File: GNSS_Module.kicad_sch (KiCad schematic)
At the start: 23 parts, among them J2 FTDI_Conn, J4 GPS_Conn, J5 GPS_Conn, U11 ublox_SAM-M8Q

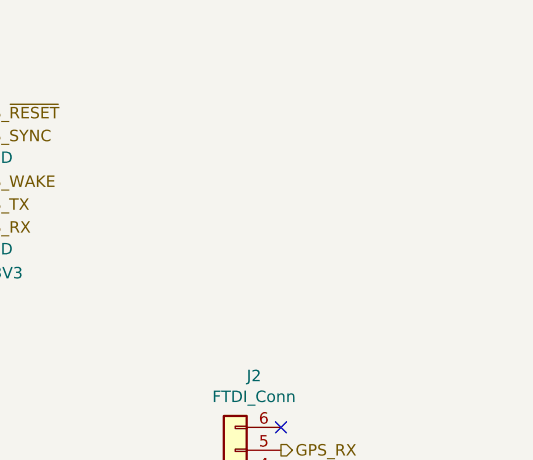
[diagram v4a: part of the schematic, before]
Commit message: (sch) add lora connector
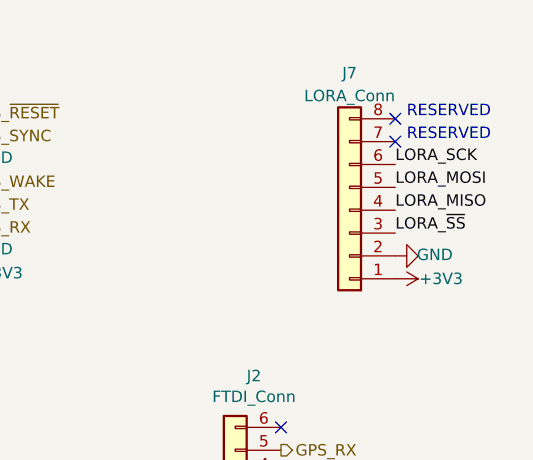
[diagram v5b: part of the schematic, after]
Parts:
- added J7: LORA_Conn, grootvoet:Connector_Amphenol_10114828-xxx08LF_Vertical, symbol Connector_Generic:Conn_01x08
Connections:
- net +3V3: now also J7.1 (Pin_1)
- net GND: now also J7.2 (Pin_2)
- new net LORA_MISO: J7.4 (Pin_4)
- new net LORA_MOSI: J7.5 (Pin_5)
- new net LORA_SCK: J7.6 (Pin_6)
- new net LORA_~{SS}: J7.3 (Pin_3)
- no-connect marks 4 -> 6
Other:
- note added: "RESERVED"
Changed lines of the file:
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@@
   (no_connect (at 231.14 74.93))
   (no_connect (at 90.17 100.33))
+  (no_connect (at 243.84 33.02))
   (no_connect (at 90.17 97.79))
+  (no_connect (at 243.84 30.48))
   (no_connect (at 231.14 64.77))
   (wire (pts (xy 90.17 92.71) (xy 109.22 92.71))
@@
     (effects (font (size 1.27 1.27)) (justify left bottom))
   )
+  (text "RESERVED" (at 245.11 33.02 0)
+    (effects (font (size 1.27 1.27)) (justify left bottom))
+  )
+  (text "RESERVED" (at 245.11 30.48 0)
+    (effects (font (size 1.27 1.27)) (justify left bottom))
+  )
   (text "GPS Power" (at 40.64 21.59 0)
     (effects (font (size 1.27 1.27) (thickness 0.254) bold) (justify left bottom))
@@
     (effects (font (size 1.27 1.27)) (justify left bottom))
   )
+  (label "LORA_~{SS}" (at 243.84 43.18 0) (fields_autoplaced)
+    (effects (font (size 1.27 1.27)) (justify left bottom))
+  )
   (label "TIMEPULSE" (at 62.23 95.25 180) (fields_autoplaced)
     (effects (font (size 1.27 1.27)) (justify right bottom))
   )
+  (label "LORA_MISO" (at 243.84 40.64 0) (fields_autoplaced)
+    (effects (font (size 1.27 1.27)) (justify left bottom))
+  )
+  (label "LORA_MOSI" (at 243.84 38.1 0) (fields_autoplaced)
+    (effects (font (size 1.27 1.27)) (justify left bottom))
+  )
   (label "TIMEPULSE" (at 177.165 62.865 0) (fields_autoplaced)
     (effects (font (size 1.27 1.27)) (justify left bottom))
   )
   (label "TIMEPULSE" (at 172.72 109.22 90) (fields_autoplaced)
+    (effects (font (size 1.27 1.27)) (justify left bottom))
+  )
+  (label "LORA_SCK" (at 243.84 35.56 0) (fields_autoplaced)
     (effects (font (size 1.27 1.27)) (justify left bottom))
   )
@@
     )
   )
+  (symbol (lib_id "power:GND") (at 243.84 45.72 90) (unit 1)
+    (in_bom yes) (on_board yes) (dnp no)
+    (property "Reference" "#PWR0141" (at 250.19 45.72 0)
+      (effects (font (size 1.27 1.27)) hide)
+    )
+    (property "Value" "GND" (at 248.2342 45.593 90)
+      (effects (font (size 1.27 1.27)))
+    )
+    (property "Footprint" "" (at 243.84 45.72 0)
+      (effects (font (size 1.27 1.27)) hide)
+    )
+    (property "Datasheet" "" (at 243.84 45.72 0)
+      (effects (font (size 1.27 1.27)) hide)
+    )
+    (pin "1")
+    (instances
+      (project "kleinvoet"
+        (path "/4185c36c-c66e-4dbd-be5d-841e551f4885/00000000-0000-0000-0000-00005edf3693"
+          (reference "#PWR0141") (unit 1)
+        )
+      )
+    )
+  )
   (symbol (lib_id "power:GND") (at 194.945 34.925 90) (unit 1)
     (in_bom yes) (on_board yes) (dnp no)
@@
     )
   )
+  (symbol (lib_id "Connector_Generic:Conn_01x08") (at 238.76 40.64 180) (unit 1)
+    (in_bom yes) (on_board yes) (dnp no) (fields_autoplaced)
+    (property "Reference" "J7" (at 238.76 25.4 0)
+      (effects (font (size 1.27 1.27)))
+    )
+    (property "Value" "LORA_Conn" (at 238.76 27.94 0)
+      (effects (font (size 1.27 1.27)))
+    )
+    (property "Footprint" "grootvoet:Connector_Amphenol_10114828-xxx08LF_Vertical" (at 238.76 40.64 0)
+      (effects (font (size 1.27 1.27)) hide)
+    )
+    (property "Datasheet" "~" (at 238.76 40.64 0)
+      (effects (font (size 1.27 1.27)) hide)
+    )
+    (pin "1")
+    (pin "2")
+    (pin "3")
+    (pin "4")
+    (pin "5")
+    (pin "6")
+    (pin "7")
+    (pin "8")
+    (instances
+      (project "kleinvoet"
+        (path "/4185c36c-c66e-4dbd-be5d-841e551f4885/00000000-0000-0000-0000-00005edf3693"
+          (reference "J7") (unit 1)
+        )
+      )
+    )
+  )
   (symbol (lib_id "power:VDD") (at 135.255 29.845 0) (unit 1)
     (in_bom yes) (on_board yes) (dnp no)
@@
         )
       )
+    )
+  )
+  (symbol (lib_id "power:+3V3") (at 243.84 48.26 270) (unit 1)
+    (in_bom yes) (on_board yes) (dnp no)
+    (property "Reference" "#PWR0143" (at 240.03 48.26 0)
+      (effects (font (size 1.27 1.27)) hide)
+    )
+    (property "Value" "+3V3" (at 248.92 48.26 90)
+      (effects (font (size 1.27 1.27)))
+    )
+    (property "Footprint" "" (at 243.84 48.26 0)
+      (effects (font (size 1.27 1.27)) hide)
+    )
+    (property "Datasheet" "" (at 243.84 48.26 0)
+      (effects (font (size 1.27 1.27)) hide)
+    )
+    (pin "1")
+    (instances
+      (project "kleinvoet"
+        (path "/4185c36c-c66e-4dbd-be5d-841e551f4885/00000000-0000-0000-0000-00005edf3693"
+          (reference "#PWR0143") (unit 1)
+        )
+      )

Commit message: big commit
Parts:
- removed J5: GPS_Conn, grootvoet:Connector_Amphenol_10114828-xxx08LF_Vertical, symbol Connector_Generic:Conn_01x08
- removed J7: LORA_Conn, grootvoet:Connector_Amphenol_10114828-xxx08LF_Vertical, symbol Connector_Generic:Conn_01x08
- removed R20: 47, Resistor_SMD:R_0603_1608Metric_Pad0.98x0.95mm_HandSolder, symbol Device:R_Small
- added C45, C46: 1u, Capacitor_SMD:C_0603_1608Metric_Pad1.08x0.95mm_HandSolder, symbol Device:C_Small
- added D7: PWR_RED, LED_SMD:LED_0603_1608Metric_Pad1.05x0.95mm_HandSolder, symbol Device:LED_Small
- added FB1: BLM18KG101TZ1D, Inductor_SMD:L_0603_1608Metric_Pad1.05x0.95mm_HandSolder, symbol Device:Ferrite_Bead_Small
- added FB12, FB14, FB15: BLM15HD102SN1, Inductor_SMD:L_0402_1005Metric, symbol Device:Ferrite_Bead_Small
- added J9: GPS_Conn, grootvoet:Connector_Amphenol_10114828-xxx08LF_Vertical, symbol Connector_Generic:Conn_01x08
- added R88: 2.2k, Resistor_SMD:R_0603_1608Metric_Pad0.98x0.95mm_HandSolder, symbol Device:R_Small
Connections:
- net +3V3: now also C45.1, FB1.2, J9.1 (Pin_1); no longer C64.1, C65.1, J2.3 (Pin_3), R3.1, R4.1, U11.17 (VCC), U11.2 (VCC_IO)
- net GND: now also C45.2, C46.2, J9.2 (Pin_2), J9.6 (Pin_6), R88.1
- net GPS_RX: now also FB12.1, J9.3 (Pin_3); no longer U11.13 (TXD)
- net GPS_SYNC: now also FB14.1, FB15.1; no longer J4.7 (Pin_7)
- net GPS_TX: now also J9.4 (Pin_4)
- net GPS_WAKE: no longer U11.19 (EXTINT)
- net GPS_~{RESET}: no longer CB40.1, R1.1, U11.18 (~{RESET})
- net GPS_~{SAFEBOOT}: no longer names the net of U11.8 (~{SAFEBOOT})
- new net: FB12.2, U11.13 (TXD)
- new net: FB15.2, J4.7 (Pin_7)
- new net: D7.1 (K), R88.2
- new net: FB14.2, J9.7 (Pin_7)
- new net +3.3V: C46.1, C64.1, C65.1, D7.2 (A), FB1.1, J2.3 (Pin_3), R3.1, R4.1, U11.17 (VCC), U11.2 (VCC_IO)
- new net GPS_INT: J9.5 (Pin_5), U11.19 (EXTINT)
- new net GPS_~{RST}: CB40.1, J9.8 (Pin_8), R1.1, U11.18 (~{RESET})
- no-connect marks 6 -> 5
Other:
- note added: "CONNECTORS"
- note added: "GNSS MODULE"
- note added: "MOUNTING HOLES"
- note added: "POWER FILTERING"
- note added: "STATUS LEDS"
- note removed: "Doesn't require a small bypass cap (100nF). There is bypass cap on the GPS daughter board close to the chip."
- note removed: "Place all components as close as possible to module. Do NOT drive RESET pin high (this will cause an reset on bootup). Keep a 10mm spacing arround module. Do not break GND plane (50x50mm)."
- note removed: "RESERVED"
- moved on the sheet: BT1, C64, C65, C66, CB40, D1, D2, D3, D4, FB10, H13, H14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

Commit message: (bc) new summation preamp & seperate power net
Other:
- moved on the sheet: D1, R2
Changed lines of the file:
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@@
     (stroke (width 0) (type default))
   )
-  (wire (pts (xy 70.485 59.055) (xy 70.485 62.23))
+  (wire (pts (xy 74.295 58.42) (xy 74.295 61.595))
     (stroke (width 0) (type default))
   )
@@
     (effects (font (size 1.27 1.27)) (justify right bottom))
   )
-  (label "TIMEPULSE" (at 70.485 59.055 90) (fields_autoplaced)
+  (label "TIMEPULSE" (at 74.295 58.42 90) (fields_autoplaced)
     (effects (font (size 1.27 1.27)) (justify left bottom))
   )
@@
     )
   )
+  (symbol (lib_id "grootvoet:GND_GNSS") (at 74.295 71.755 0) (unit 1)
+    (in_bom yes) (on_board yes) (dnp no) (fields_autoplaced)
+    (property "Reference" "#PWR094" (at 74.295 78.105 0)
+      (effects (font (size 1.27 1.27)) hide)
+    )
+    (property "Value" "GND_GNSS" (at 74.295 76.835 0)
+      (effects (font (size 1.27 1.27)))
+    )
+    (property "Footprint" "" (at 74.295 71.755 0)
+      (effects (font (size 1.27 1.27)) hide)
+    )
+    (property "Datasheet" "" (at 74.295 71.755 0)
+      (effects (font (size 1.27 1.27)) hide)
+    )
+    (pin "1")
+    (instances
+      (project "kleinvoet"
+        (path "/4185c36c-c66e-4dbd-be5d-841e551f4885/00000000-0000-0000-0000-00005edf3693"
+          (reference "#PWR094") (unit 1)
+        )
+      )
+    )
+  )
   (symbol (lib_id "grootvoet:GND_GNSS") (at 22.86 35.56 0) (unit 1)
     (in_bom yes) (on_board yes) (dnp no) (fields_autoplaced)
@@
     )
   )
-  (symbol (lib_id "Device:R_Small") (at 70.485 64.77 0) (mirror x) (unit 1)
-    (in_bom yes) (on_board yes) (dnp no)
-    (property "Reference" "R2" (at 71.9836 65.9384 0)
-      (effects (font (size 1.27 1.27)) (justify left))
-    )
-    (property "Value" "2.2k" (at 71.9836 63.627 0)
-      (effects (font (size 1.27 1.27)) (justify left))
-    )
-    (property "Footprint" "Resistor_SMD:R_0603_1608Metric_Pad0.98x0.95mm_HandSolder" (at 70.485 64.77 0)
-      (effects (font (size 1.27 1.27)) hide)
-    )
-    (property "Datasheet" "~" (at 70.485 64.77 0)
-      (effects (font (size 1.27 1.27)) hide)
-    )
-    (property "MPN" "RC0603FR-072K2L" (at 70.485 64.77 0)
-      (effects (font (size 1.27 1.27)) hide)
-    )
-    (property "Mfr." "Yageo" (at 70.485 64.77 0)
+  (symbol (lib_id "Device:R_Small") (at 74.295 64.135 0) (mirror x) (unit 1)
+    (in_bom yes) (on_board yes) (dnp no)
+    (property "Reference" "R2" (at 75.7936 65.3034 0)
+      (effects (font (size 1.27 1.27)) (justify left))
+    )
+    (property "Value" "2.2k" (at 75.7936 62.992 0)
+      (effects (font (size 1.27 1.27)) (justify left))
+    )
+    (property "Footprint" "Resistor_SMD:R_0603_1608Metric_Pad0.98x0.95mm_HandSolder" (at 74.295 64.135 0)
+      (effects (font (size 1.27 1.27)) hide)
+    )
+    (property "Datasheet" "~" (at 74.295 64.135 0)
+      (effects (font (size 1.27 1.27)) hide)
+    )
+    (property "MPN" "RC0603FR-072K2L" (at 74.295 64.135 0)
+      (effects (font (size 1.27 1.27)) hide)
+    )
+    (property "Mfr." "Yageo" (at 74.295 64.135 0)
       (effects (font (size 1.27 1.27)) hide)
     )
@@
     )
   )
-  (symbol (lib_id "Device:LED_Small") (at 70.485 69.85 90) (unit 1)
-    (in_bom yes) (on_board yes) (dnp no)
-    (property "Reference" "D1" (at 72.263 68.6816 90)
+  (symbol (lib_id "Device:LED_Small") (at 74.295 69.215 90) (unit 1)
+    (in_bom yes) (on_board yes) (dnp no)
+    (property "Reference" "D1" (at 76.073 68.0466 90)
       (effects (font (size 1.27 1.27)) (justify right))
     )
-    (property "Value" "BLUE" (at 72.263 70.993 90)
+    (property "Value" "BLUE" (at 76.073 70.358 90)
       (effects (font (size 1.27 1.27)) (justify right))
     )
-    (property "Footprint" "LED_SMD:LED_0603_1608Metric_Pad1.05x0.95mm_HandSolder" (at 70.485 69.85 90)
-      (effects (font (size 1.27 1.27)) hide)
-    )
-    (property "Datasheet" "~" (at 70.485 69.85 90)
-      (effects (font (size 1.27 1.27)) hide)
-    )
-    (property "MPN" "SMLD12BN1WT86" (at 70.485 69.85 90)
-      (effects (font (size 1.27 1.27)) hide)
-    )
-    (property "Mfr." "ROHM Semiconductor" (at 70.485 69.85 90)
+    (property "Footprint" "LED_SMD:LED_0603_1608Metric_Pad1.05x0.95mm_HandSolder" (at 74.295 69.215 90)
+      (effects (font (size 1.27 1.27)) hide)
+    )
+    (property "Datasheet" "~" (at 74.295 69.215 90)
+      (effects (font (size 1.27 1.27)) hide)
+    )
+    (property "MPN" "SMLD12BN1WT86" (at 74.295 69.215 90)
+      (effects (font (size 1.27 1.27)) hide)
+    )
+    (property "Mfr." "ROHM Semiconductor" (at 74.295 69.215 90)
       (effects (font (size 1.27 1.27)) hide)
     )
@@
         )
       )
-    )
-  )
-  (symbol (lib_id "power:GND") (at 70.485 72.39 0) (unit 1)
-    (in_bom yes) (on_board yes) (dnp no)
-    (property "Reference" "#PWR017" (at 70.485 78.74 0)
-      (effects (font (size 1.27 1.27)) hide)
-    )
-    (property "Value" "GND" (at 70.612 76.7842 0)
-      (effects (font (size 1.27 1.27)))
-    )
-    (property "Footprint" "" (at 70.485 72.39 0)
-      (effects (font (size 1.27 1.27)) hide)
-    )
-    (property "Datasheet" "" (at 70.485 72.39 0)
-      (effects (font (size 1.27 1.27)) hide)
-    )
-    (pin "1")
-    (instances
-      (project "kleinvoet"
-        (path "/4185c36c-c66e-4dbd-be5d-841e551f4885"
-          (reference "#PWR017") (unit 1)
-        )
-        (path "/4185c36c-c66e-4dbd-be5d-841e551f4885/00000000-0000-0000-0000-00005edf3693"
-          (reference "#PWR094") (unit 1)
-        )
-      )

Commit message: (bc) changes for the day
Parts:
- removed CB40: 100n, Capacitor_SMD:C_0603_1608Metric_Pad1.08x0.95mm_HandSolder, symbol Device:C_Small
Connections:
- net GPS_~{RESET} is gone; now on net GND: J4.8 (Pin_8)
- net +3.3V: now also R1.1
- net GND: now also J9.8 (Pin_8); no longer R1.2
- removed net GPS_~{RST}: J9.8 (Pin_8), R1.1, U11.18 (~{RESET})
- new net: R1.2, U11.18 (~{RESET})
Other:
- moved on the sheet: FB10, FB12, FB15, J4, R1, U11
